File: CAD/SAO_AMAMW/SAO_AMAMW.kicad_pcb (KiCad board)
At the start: 2 copper layers, 55.3 x 71.6 mm, 34 parts, among them J1 Badgelife_sao_connector_v169b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, U1 TPS61023

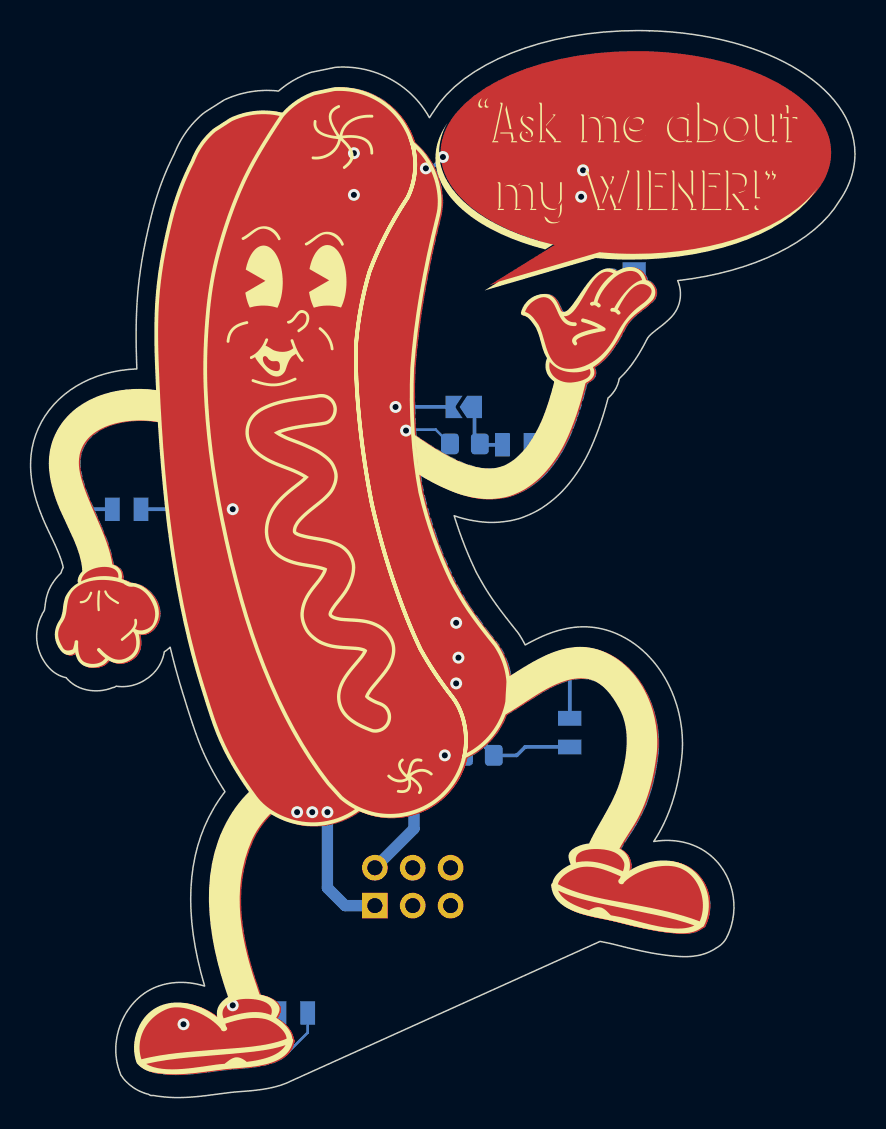
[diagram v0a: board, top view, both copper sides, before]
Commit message: Updates with new SAO footprint
Updated SAO Footprint. Moved LEDs so they all have the same orientation.
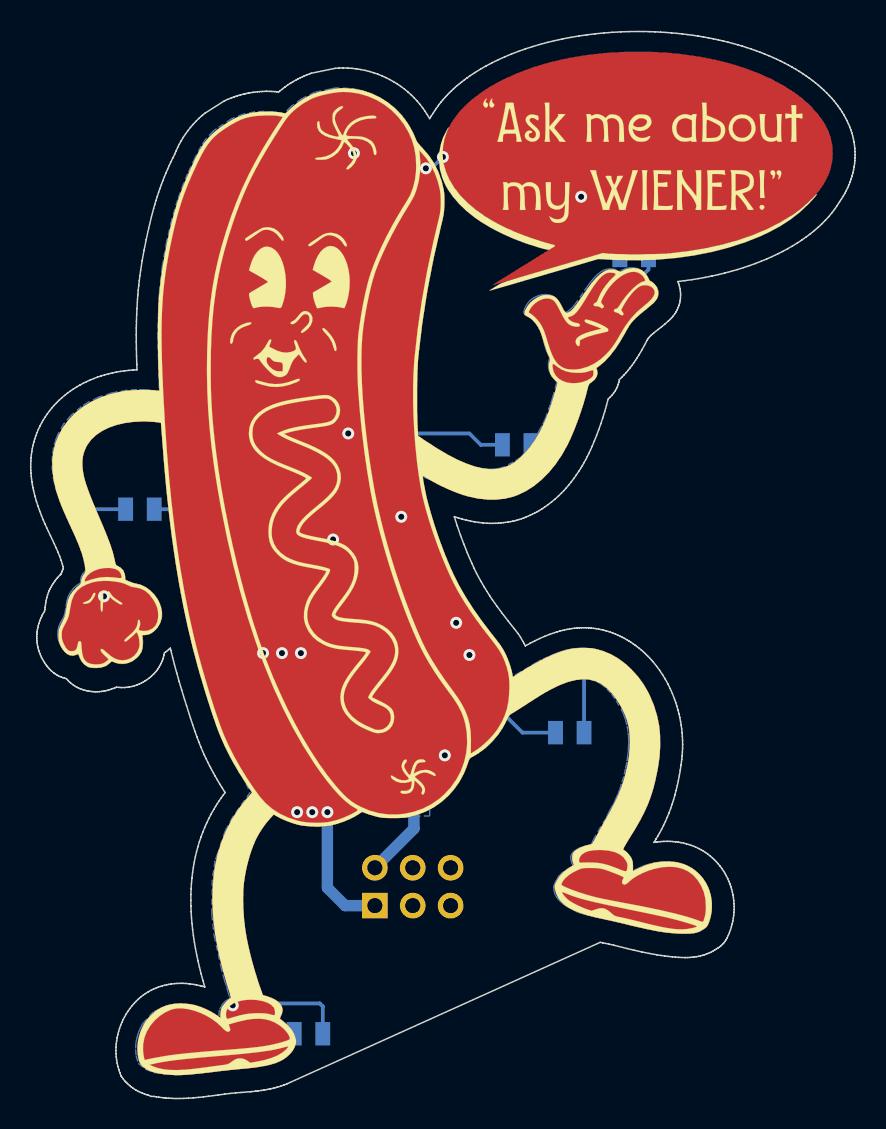
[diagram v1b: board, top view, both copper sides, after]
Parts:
- removed JP1, JP2, JP3, JP4, JP5, JP7: SolderJumper_2_Open, Jumper:SolderJumper-2_P1.3mm_Open_TrianglePad1.0x1.5mm
- X1: footprint BadgePirates:AMAMW -> drawing:AMAMW
- moved R2 7.61 mm to (119.3, 95.2), turned to -78 degrees
- moved X1 6.80 mm to (139.6, 54.7)
- moved R4 5.46 mm to (138.4, 86.6)
- moved C2 3.41 mm to (132.8, 98.3), turned to -90 degrees
- moved R3 2.90 mm to (144.0, 105.4)
- moved D6 1.73 mm to (133.3, 126.9), turned to 0 degrees
- moved C5 1.35 mm to (139.6, 94.5), turned to 90 degrees
- moved C3 1.01 mm to (130.4, 98.3), turned to -90 degrees
- moved D2 0.89 mm to (122.0, 91.7), turned to 0 degrees
- turned D3 to 0 degrees
- turned D5 to 0 degrees
- turned R10 to 0 degrees
- turned R9 to 180 degrees
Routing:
- net /EN: track 0.00 -> 7.44 mm
- net GND: track 33.9 -> 27.0 mm
- net /SW_FB: track 0.00 -> 5.52 mm
- net Net-(D6-K): track 8.74 -> 4.48 mm
- net Net-(D4-K): track 3.66 -> 7.25 mm
- net Net-(D3-K): track 8.34 -> 5.42 mm
- net Net-(D1-K): track 4.96 -> 2.56 mm
- net +3V6: track 18.7 -> 17.3 mm
- net Net-(D5-K): track 5.38 -> 4.75 mm
- net Net-(D2-K): track 5.63 -> 5.04 mm
- added copper zone on B.Cu, net +3.3V
- added copper zone on B.Cu, net /SW_SW
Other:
- outline, holes or cut-outs redrawn
